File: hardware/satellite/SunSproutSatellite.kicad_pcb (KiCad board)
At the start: 4 copper layers, 27.2 x 51.1 mm, 46 parts, among them J1 RJHSE5380_QwiicBusCompatible, J2 Conn_01x03, J3 Conn_01x03, J4 Conn_01x03, J5 Conn_01x03, J6 Conn_01x03, J7 Conn_01x04, J8 Qwiic, J9 Conn_01x04, U1 PCA9615DPZ, U2 ADS1115IDGS, U3 DS2482S-100+, U4 USBLC6-4SC6

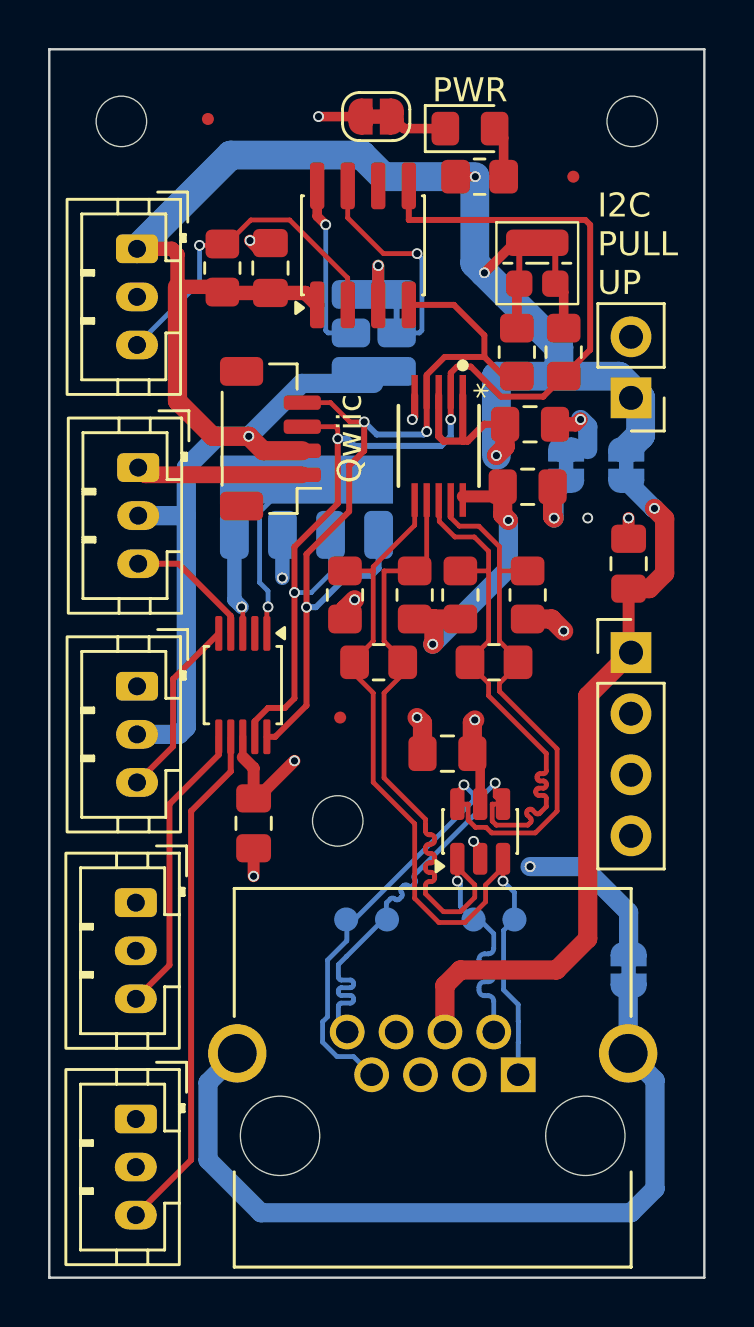
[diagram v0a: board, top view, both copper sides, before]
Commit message: hardware(satellite): larger  pull up solder jumper Fix model for PCA9615DPZ so it renders correctly
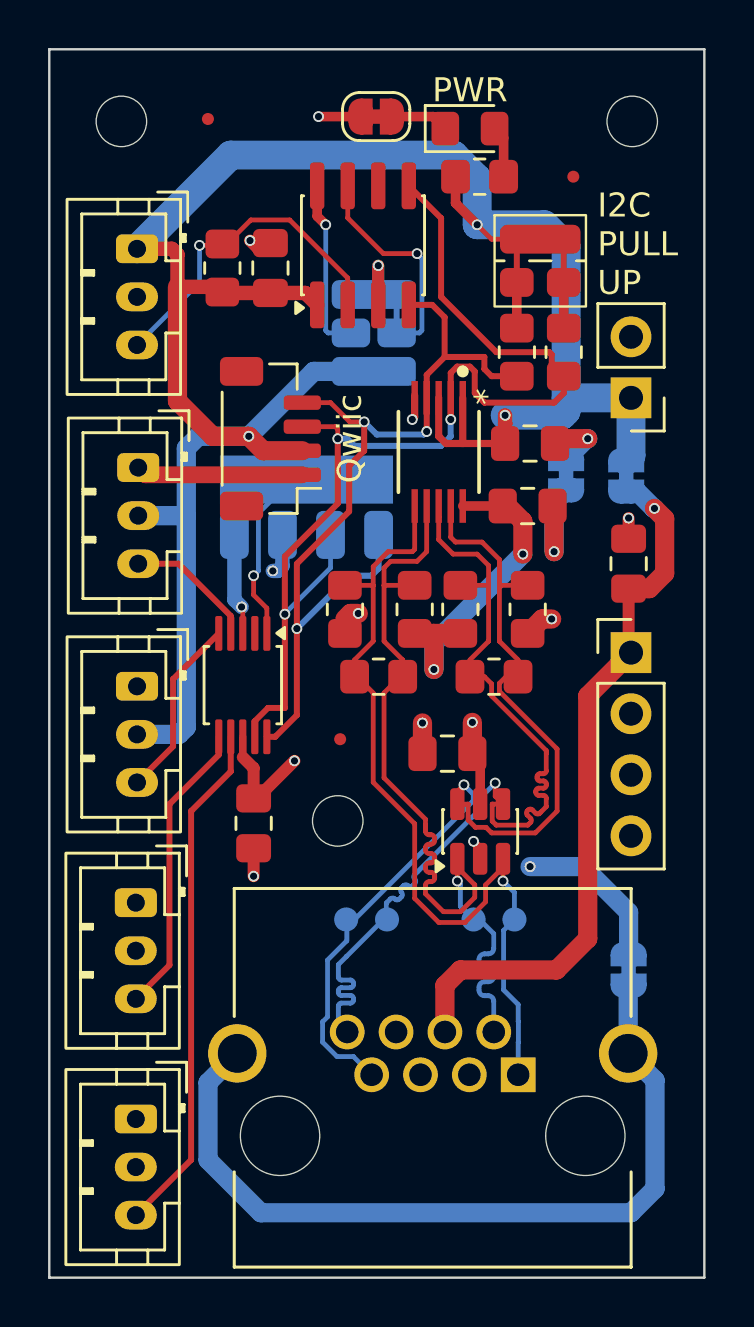
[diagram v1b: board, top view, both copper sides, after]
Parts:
- moved Ref** 0.90 mm to (112.1, 128.7)
- moved C2 0.80 mm to (120.0, 116.4)
- moved C3 0.80 mm to (119.9, 119.0)
- moved R3 0.60 mm to (115.2, 123.3)
- moved R4 0.60 mm to (113.7, 126.1)
- moved R5 0.60 mm to (112.3, 123.3)
- moved R6 0.60 mm to (117.1, 123.3)
- moved R7 0.60 mm to (118.5, 126.1)
- moved R8 0.60 mm to (119.9, 123.3)
- moved JP18 0.45 mm to (124.0, 117.8)
- moved JP17 0.40 mm to (121.5, 117.7)
- moved U1 0.25 mm to (116.2, 116.8)
- moved JP11 0.16 mm to (120.4, 108.8)
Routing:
- net SAT_3V3: track 147.4 -> 149.6 mm, vias 6 -> 5
- net SDA_LOCAL: track 48.7 -> 46.6 mm
- net RJ45_VCC_1: track 57.9 -> 59.1 mm
- net DSCL_P: track 34.7 -> 35.7 mm
- net RJ45_GND_1: track 15.7 -> 16.4 mm, vias 8 -> 7
